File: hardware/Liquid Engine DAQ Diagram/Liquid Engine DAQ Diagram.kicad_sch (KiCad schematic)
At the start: 44 parts, among them J1 Conn_01x14_Pin, J10 Conn_01x14_Pin, J11 Conn_01x24_Pin, J12 Conn_01x24_Pin, J13 Conn_01x06_Pin, J14 Conn_01x06_Pin, J15 Conn_01x04_Pin, J16 Conn_01x04_Pin, J17 Conn_01x03_Pin, J18 Conn_01x03_Pin, J19 Conn_01x03_Pin, J2 Conn_01x14_Pin, J20 Conn_01x03_Pin, J21 Conn_01x03_Pin, J22 Conn_01x03_Pin, J23 Conn_01x03_Pin, J24 Conn_01x03_Pin, J25 Conn_01x16_Pin, J26 Conn_01x06_Pin, J27 Conn_01x06_Pin, J28 Conn_01x02_Pin, J29 Conn_01x02_Pin, J3 Conn_01x05_Pin, J30 Conn_01x02_Pin, J31 Conn_01x02_Pin, J32 Conn_01x06_Pin, J33 Conn_01x06_Pin, J34 Conn_01x08_Pin, J35 Conn_01x08_Pin, J36 Conn_01x05_Pin, J37 Conn_01x04_Pin, J38 Conn_01x06_Pin, J39 Conn_01x06_Pin, J4 Conn_01x08_Pin, J40 Conn_01x08_Pin, J41 Conn_01x08_Pin, J5 Conn_01x08_Pin, J6 DIN41612_02x08_AB_EvenPins, J7 Conn_01x14_Pin, J8 Conn_01x08_Pin, J9 Conn_01x05_Pin

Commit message: updated files and created platformio projects for microcontrollers
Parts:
- added CN10: Conn_02x17_Odd_Even, symbol Connector_Generic:Conn_02x17_Odd_Even
- added CN7: Conn_02x10_Odd_Even, symbol Connector_Generic:Conn_02x10_Odd_Even
- added CN8: Conn_02x08_Odd_Even, symbol Connector_Generic:Conn_02x08_Odd_Even
- added CN9: Conn_02x15_Odd_Even, symbol Connector_Generic:Conn_02x15_Odd_Even
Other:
- note added: "Nucleo-H755ZI-Q"

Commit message: updated circuit diagram, fixed firmware project folder, added tbeam pinout
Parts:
- removed BT1: Batt, symbol Device:Battery
- removed J11, J12: Conn_01x24_Pin, symbol Connector:Conn_01x24_Pin
- removed J36: Conn_01x05_Pin, symbol Connector:Conn_01x05_Pin
- added J11: Conn_01x09_Pin, symbol Connector:Conn_01x09_Pin
- added J12, J36, J42: Conn_01x02_Pin, symbol Connector:Conn_01x02_Pin
- added J43: Conn_01x04_Pin, symbol Connector:Conn_01x04_Pin
- added J44: CN11, symbol Connector:Conn_01x02_Pin
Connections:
- net at J1.VIN, J10.VIN, J14.1 (VCC)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: now also J44.6 (5V_EXT)
- net at BT2.2 (-), J1.GND, J10.GND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: now also J37.1 (GND), J6.ACOM0, J6.ACOM1, J6.ACOM2, J6.ACOM3, J6.ACOM4, J6.ACOM5, J6.ACOM6, J6.ACOM7, J11.2 (GND), J36.GND, J44.8 (GND)
- net at BT2.1 (+), J15.3 (VIN): now also J37.3 (VIN)
- net at J35.VM: no longer J33.LV
- net at J10.13: now also CN7.10 (Pin_10)
- net at J1.13: now also CN7.15 (Pin_15)
- net at J7.10: now also CN7.16 (Pin_16)
- net at J7.12: now also CN7.12 (Pin_12)
- net at J2.10: now also CN7.17 (Pin_17)
- net at J2.11: now also CN7.13 (Pin_13)
- net at J2.12: now also CN7.19 (Pin_19)
- net at J7.11: now also CN7.14 (Pin_14)
- net at CN8.11 (Pin_11): now also J43.GND (Pin_1)
- net at CN8.5 (Pin_5): now also J43.RST (Pin_4)
- net at CN8.9 (Pin_9): now also J43.5V (Pin_2)
- net at CN10.13 (Pin_13): now also J11.6 (D3/CS)
- net at CN10.14 (Pin_14): now also J12.RX
- net at CN10.15 (Pin_15): now also J11.3 (CLK)
- net at CN10.16 (Pin_16): now also J12.TX
- net at CN10.21 (Pin_21): now also J11.4 (D0/SO)
- net at CN10.23 (Pin_23): now also J11.5 (CMD/SI)
- net at CN7.2 (Pin_2): now also J42.SCL
- net at CN7.4 (Pin_4): now also J42.SDA
- new net: J11.1 (3V), J36.3V3, J37.2 (3V)
- now unconnected: J3.3.3V, J3.GND, J9.3.3V, J9.GND
- no-connect marks 15 -> 19
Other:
- note added: "6V DC Power Supply"
- note added: "ESP32 T-Beam"
- note added: "For the QSPI pins on the Nucleo board: Google AI results say that Data0 = MOSI and Data1 = MISO when operating QSPI in single SPI mode, however, I can't find anything to definitively confirm that."
- note added: "Micro SD SPI/SDIO Breakout Board (SPI config)"
- note added: "No longer sure that we need this logic level shifter. ADS1256 digital pins may be 3.3V, not completely sure. Also what voltage for VM? Would probably have to take the 3.3V directly from Teensy?"
- note added: "Not exactly sure where the LV should come from. Probably the 3.3V from the Teensy?"
- note added: "Reset pin connection probably not needed!"
- note added: "Servo Shield"
- note added: "When using external power, jumper JP2 must be on pin 5-6 EXT."
- note removed: "2x AA"
- note removed: "7.4V 2.6Ah 2S Li-Ion 18650"
- note removed: "Teensy 4.1"
- moved on the sheet: CN10, CN7, CN8, CN9

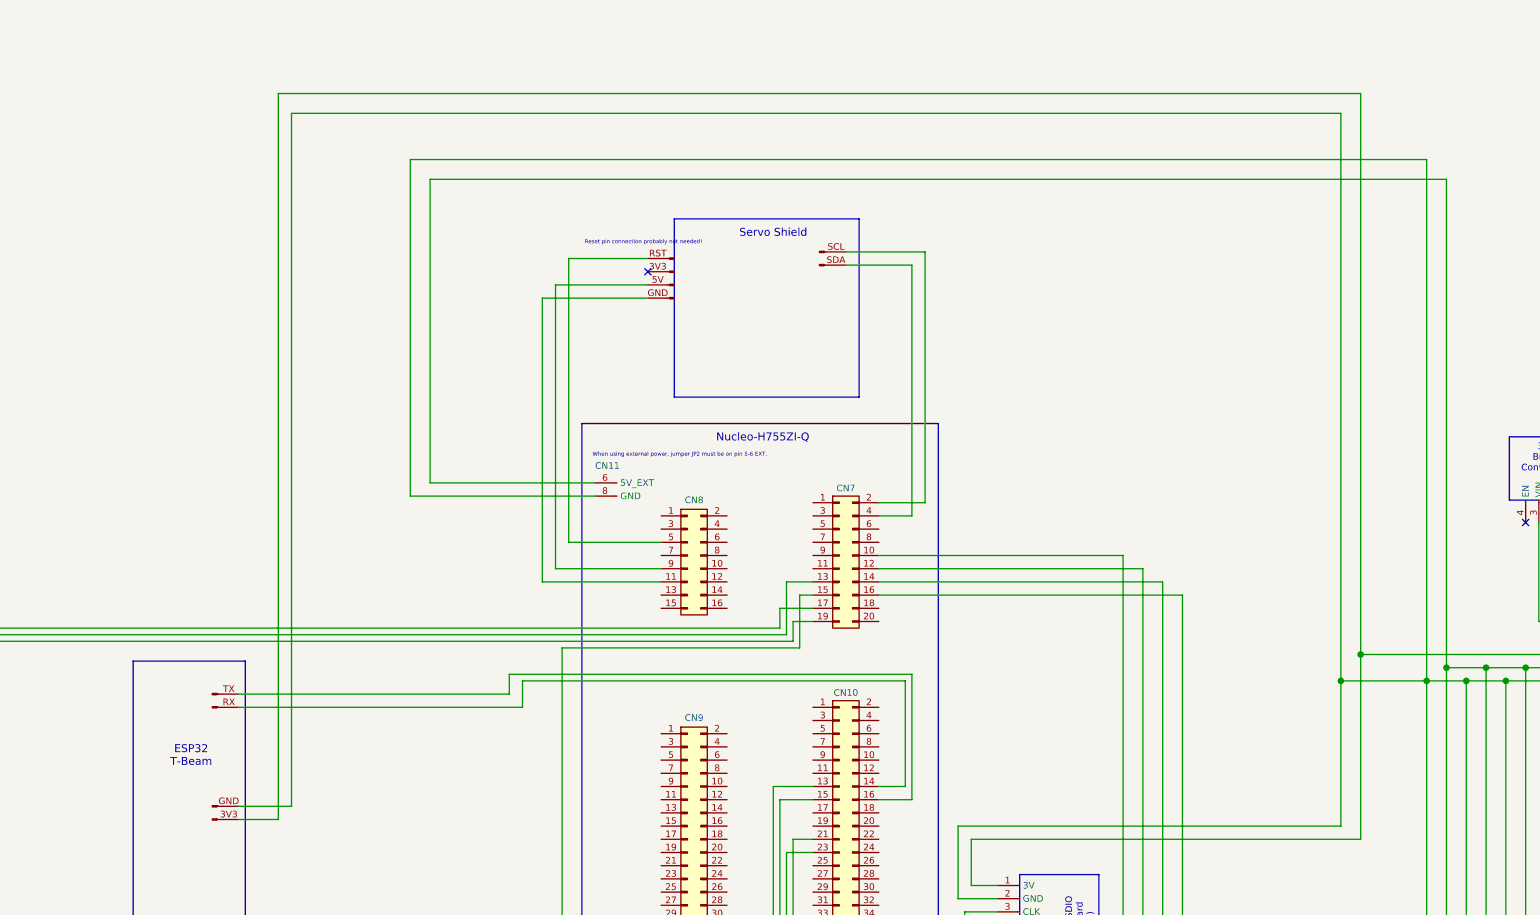
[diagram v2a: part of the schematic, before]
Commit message: updated circuit diagram
- Tbeam powered using 5V, not 3V
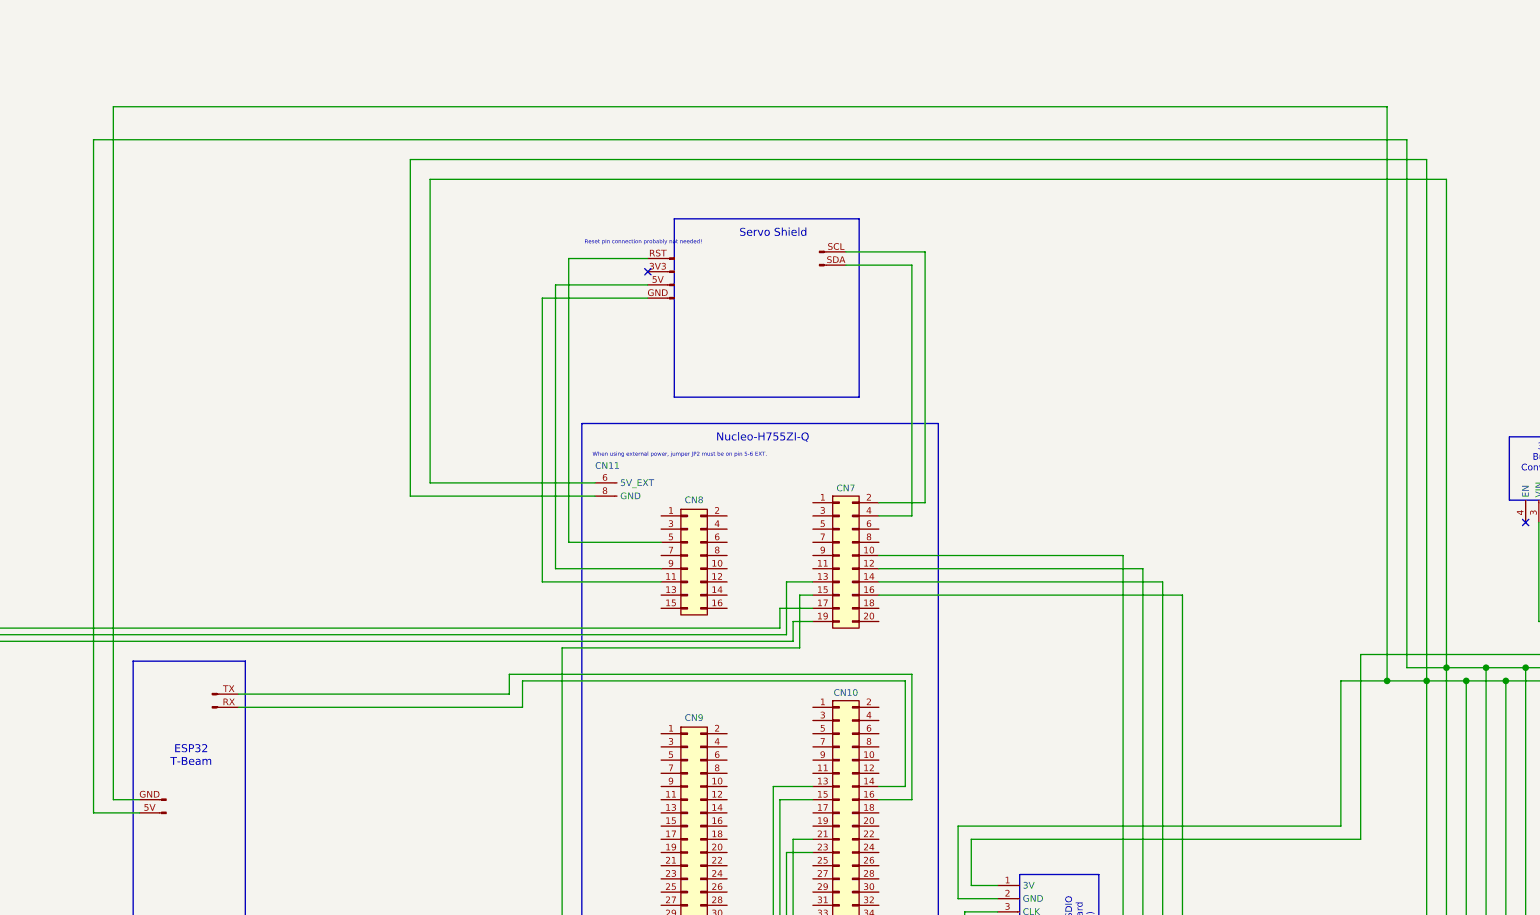
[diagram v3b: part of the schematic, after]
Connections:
- net at J1.VIN, J10.VIN, J14.1 (VCC)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: now also J36.5V
- net at J11.1 (3V), J37.2 (3V): no longer J36.3V3
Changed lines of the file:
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@@
 	(paper "A2")
 	(junction
+		(at 364.49 186.69)
+		(diameter 1.27)
+		(color 0 0 0 1)
+	)
+	(junction
 		(at 52.07 326.39)
 		(diameter 1.27)
@@
 	)
 	(junction
-		(at 355.6 186.69)
-		(diameter 1.27)
-		(color 0 0 0 1)
-	)
-	(junction
-		(at 359.41 181.61)
-		(diameter 1.27)
-		(color 194 0 0 1)
-	)
-	(junction
 		(at 372.11 186.69)
 		(diameter 1.27)
@@
 	(wire
 		(pts
+			(xy 115.57 82.55) (xy 115.57 212.09)
+		)
+		(stroke
+			(width 0.4064)
+			(type default)
+			(color 255 0 0 1)
+		)
+	)
+	(wire
+		(pts
 			(xy 481.33 261.62) (xy 481.33 273.05)
 		)
@@
 	(wire
 		(pts
-			(xy 372.11 186.69) (xy 355.6 186.69)
+			(xy 372.11 186.69) (xy 364.49 186.69)
 		)
 		(stroke
@@
 	(wire
 		(pts
+			(xy 115.57 212.09) (xy 124.46 212.09)
+		)
+		(stroke
+			(width 0.4064)
+			(type default)
+			(color 255 0 0 1)
+		)
+	)
+	(wire
+		(pts
 			(xy 48.26 283.21) (xy 52.07 283.21)
 		)
@@
 	(wire
 		(pts
-			(xy 359.41 181.61) (xy 359.41 73.66)
-		)
-		(stroke
-			(width 0.4064)
-			(type default)
-			(color 194 0 0 1)
-		)
-	)
-	(wire
-		(pts
 			(xy 541.02 254) (xy 537.21 254)
 		)
@@
 	(wire
 		(pts
-			(xy 151.13 213.36) (xy 143.51 213.36)
-		)
-		(stroke
-			(width 0.4064)
-			(type default)
-			(color 194 0 0 1)
-		)
-	)
-	(wire
-		(pts
 			(xy 248.92 219.71) (xy 248.92 236.22)
 		)
@@
 	(wire
 		(pts
-			(xy 151.13 73.66) (xy 151.13 213.36)
-		)
-		(stroke
-			(width 0.4064)
-			(type default)
-			(color 194 0 0 1)
-		)
-	)
-	(wire
-		(pts
 			(xy 476.25 283.21) (xy 469.9 283.21)
 		)
@@
 	(wire
 		(pts
+			(xy 368.3 82.55) (xy 115.57 82.55)
+		)
+		(stroke
+			(width 0.4064)
+			(type default)
+			(color 255 0 0 1)
+		)
+	)
+	(wire
+		(pts
 			(xy 222.25 113.03) (xy 201.93 113.03)
 		)
@@
 	(wire
 		(pts
+			(xy 119.38 209.55) (xy 124.46 209.55)
+		)
+		(stroke
+			(width 0.4064)
+			(type default)
+			(color 0 0 0 1)
+		)
+	)
+	(wire
+		(pts
 			(xy 60.96 -24.13) (xy 60.96 -57.15)
 		)
@@
 	(wire
 		(pts
-			(xy 398.78 186.69) (xy 415.29 186.69)
+			(xy 364.49 186.69) (xy 355.6 186.69)
 		)
 		(stroke
@@
 	(wire
 		(pts
-			(xy 359.41 73.66) (xy 151.13 73.66)
+			(xy 398.78 186.69) (xy 415.29 186.69)
 		)
 		(stroke
 			(width 0.4064)
 			(type default)
-			(color 194 0 0 1)
+			(color 0 0 0 1)
 		)
 	)
@@
 	(wire
 		(pts
-			(xy 153.67 77.47) (xy 153.67 210.82)
+			(xy 119.38 76.2) (xy 119.38 209.55)
 		)
 		(stroke
@@
 	(wire
 		(pts
+			(xy 364.49 76.2) (xy 364.49 186.69)
+		)
+		(stroke
+			(width 0.4064)
+			(type default)
+			(color 0 0 0 1)
+		)
+	)
+	(wire
+		(pts
 			(xy 120.65 248.92) (xy 120.65 259.08)
 		)
@@
 	(wire
 		(pts
-			(xy 355.6 77.47) (xy 153.67 77.47)
+			(xy 119.38 76.2) (xy 364.49 76.2)
 		)
 		(stroke
@@
 	(wire
 		(pts
+			(xy 375.92 184.15) (xy 368.3 184.15)
+		)
+		(stroke
+			(width 0.4064)
+			(type default)
+			(color 255 0 0 1)
+		)
+	)
+	(wire
+		(pts
 			(xy 55.88 312.42) (xy 55.88 302.26)
 		)
@@
 	(wire
 		(pts
-			(xy 355.6 186.69) (xy 355.6 77.47)
-		)
-		(stroke
-			(width 0.4064)
-			(type default)
-			(color 0 0 0 1)
-		)
-	)
-	(wire
-		(pts
 			(xy 222.25 105.41) (xy 207.01 105.41)
 		)
@@
 	(wire
 		(pts
-			(xy 153.67 210.82) (xy 143.51 210.82)
-		)
-		(stroke
-			(width 0.4064)
-			(type default)
-			(color 0 0 0 1)
-		)
-	)
-	(wire
-		(pts
 			(xy 398.78 288.29) (xy 317.5 288.29)
 		)
@@
 	(wire
 		(pts
+			(xy 368.3 184.15) (xy 368.3 82.55)
+		)
+		(stroke
+			(width 0.4064)
+			(type default)
+			(color 255 0 0 1)
+		)
+	)
+	(wire
+		(pts
 			(xy 260.35 104.14) (xy 275.59 104.14)
 		)
@@
 		(lib_name "Conn_01x02_Pin_2")
 		(lib_id "Connector:Conn_01x02_Pin")
-		(at 138.43 210.82 0)
+		(at 129.54 212.09 180)
 		(unit 1)
 		(exclude_from_sim no)
@@
 		(fields_autoplaced yes)
 		(property "Reference" "J36"
-			(at 139.065 207.01 0)
+			(at 128.905 215.9 0)
 			(effects
 				(font
@@
 		)
 		(property "Value" "Conn_01x02_Pin"
-			(at 139.065 209.55 0)
+			(at 128.905 213.36 0)
 			(effects
 				(font
@@
 		)
 		(property "Footprint" ""
-			(at 138.43 210.82 0)
+			(at 129.54 212.09 0)
 			(effects
 				(font
@@
 		)
 		(property "Datasheet" "~"
-			(at 138.43 210.82 0)
+			(at 129.54 212.09 0)
 			(effects
 				(font
@@
 		)
 		(property "Description" "Generic connector, single row, 01x02, script generated"
-			(at 138.43 210.82 0)
+			(at 129.54 212.09 0)
 			(effects
 				(font
@@
 			)
 		)
-		(pin "3V3"
+		(pin "5V"
 		)
 		(pin "GND"

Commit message: updated circuit diagram to reflect updates and actual solder connections
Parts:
- removed J34, J35: Conn_01x08_Pin, symbol Connector:Conn_01x08_Pin
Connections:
- net at BT2.2 (-), J1.GND, J10.GND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: no longer J5.DOUT
- net at J5.SCLK: now also J1.13
- net at J5.CS: now also J2.10
- net at J5.DIN: now also J2.11
- net at J4.37: now also CN7.10 (Pin_10)
- net at J4.36: now also CN7.16 (Pin_16)
- net at J4.34: now also CN7.12 (Pin_12)
- net at J4.35: now also CN7.14 (Pin_14)
- net at J10.13: now also CN7.15 (Pin_15); no longer CN7.10 (Pin_10)
- net at CN7.17 (Pin_17): now also J7.10; no longer J2.10
- net at CN7.13 (Pin_13): now also J7.11; no longer J2.11
- net at J2.12: now also J5.DOUT; no longer CN7.19 (Pin_19)
- net at J7.12: now also CN7.19 (Pin_19); no longer CN7.12 (Pin_12)
- no-connect marks 19 -> 15
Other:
- note removed: "No longer sure that we need this logic level shifter. ADS1256 digital pins may be 3.3V, not completely sure. Also what voltage for VM? Would probably have to take the 3.3V directly from Teensy?"
- note removed: "Peripheral | Serial"
- moved on the sheet: CN10, CN7, CN8, CN9
